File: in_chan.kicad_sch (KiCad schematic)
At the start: 7 parts, among them U7 MAX31910AUI+

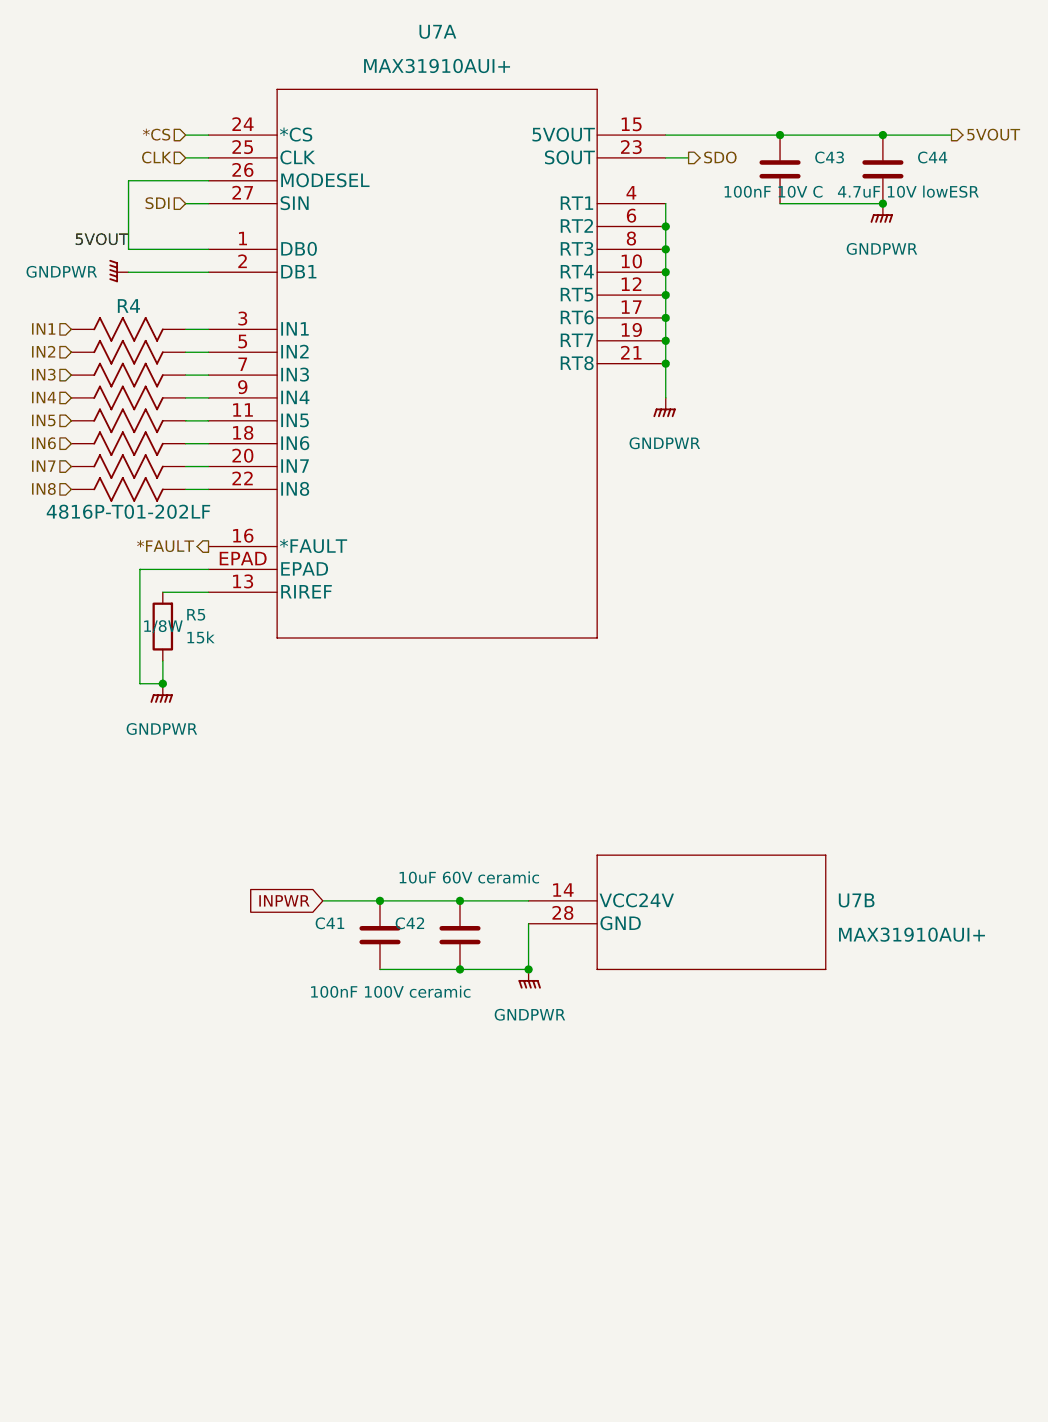
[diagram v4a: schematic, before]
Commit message: add zeners in the meantime, if the SPI isolator is delayed
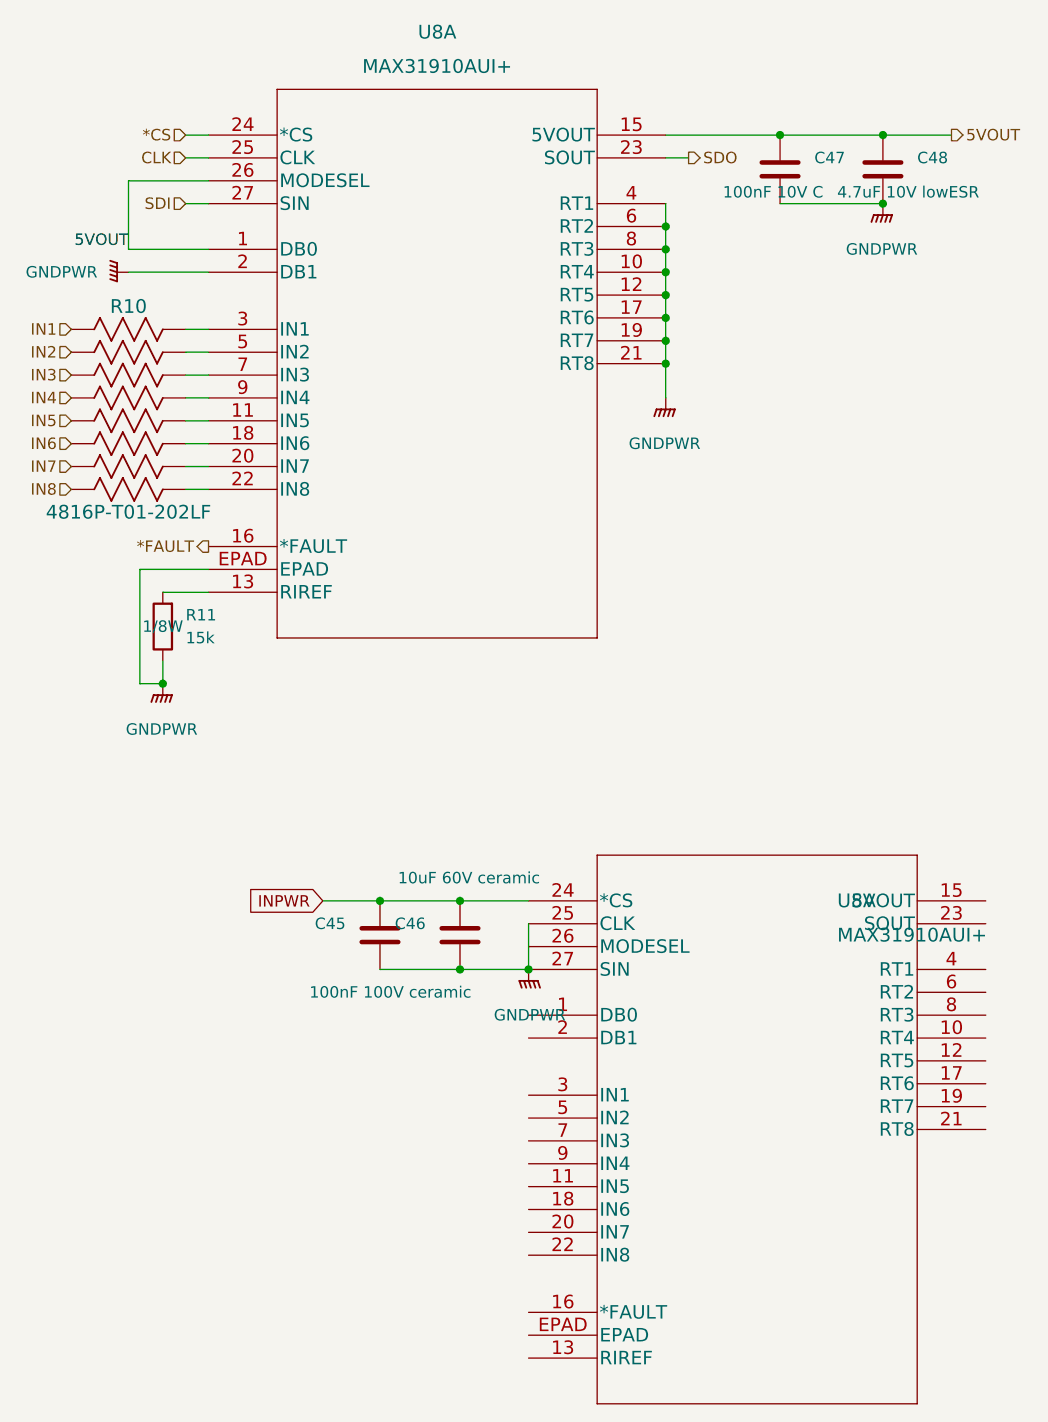
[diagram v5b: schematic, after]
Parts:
- renumbered C41 to C45, C42 to C46, C43 to C47, C44 to C48, R4 to R10, R5 to R11, U7 to U8
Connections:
- net GNDPWR: now also U8.25 (CLK), U8.27 (SIN); no longer U8.28 (GND)
- net INPWR: now also U8.24 (*CS); no longer U8.14 (VCC24V)

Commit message: fixes after V1
4 resistors for input power
disable CRCEN
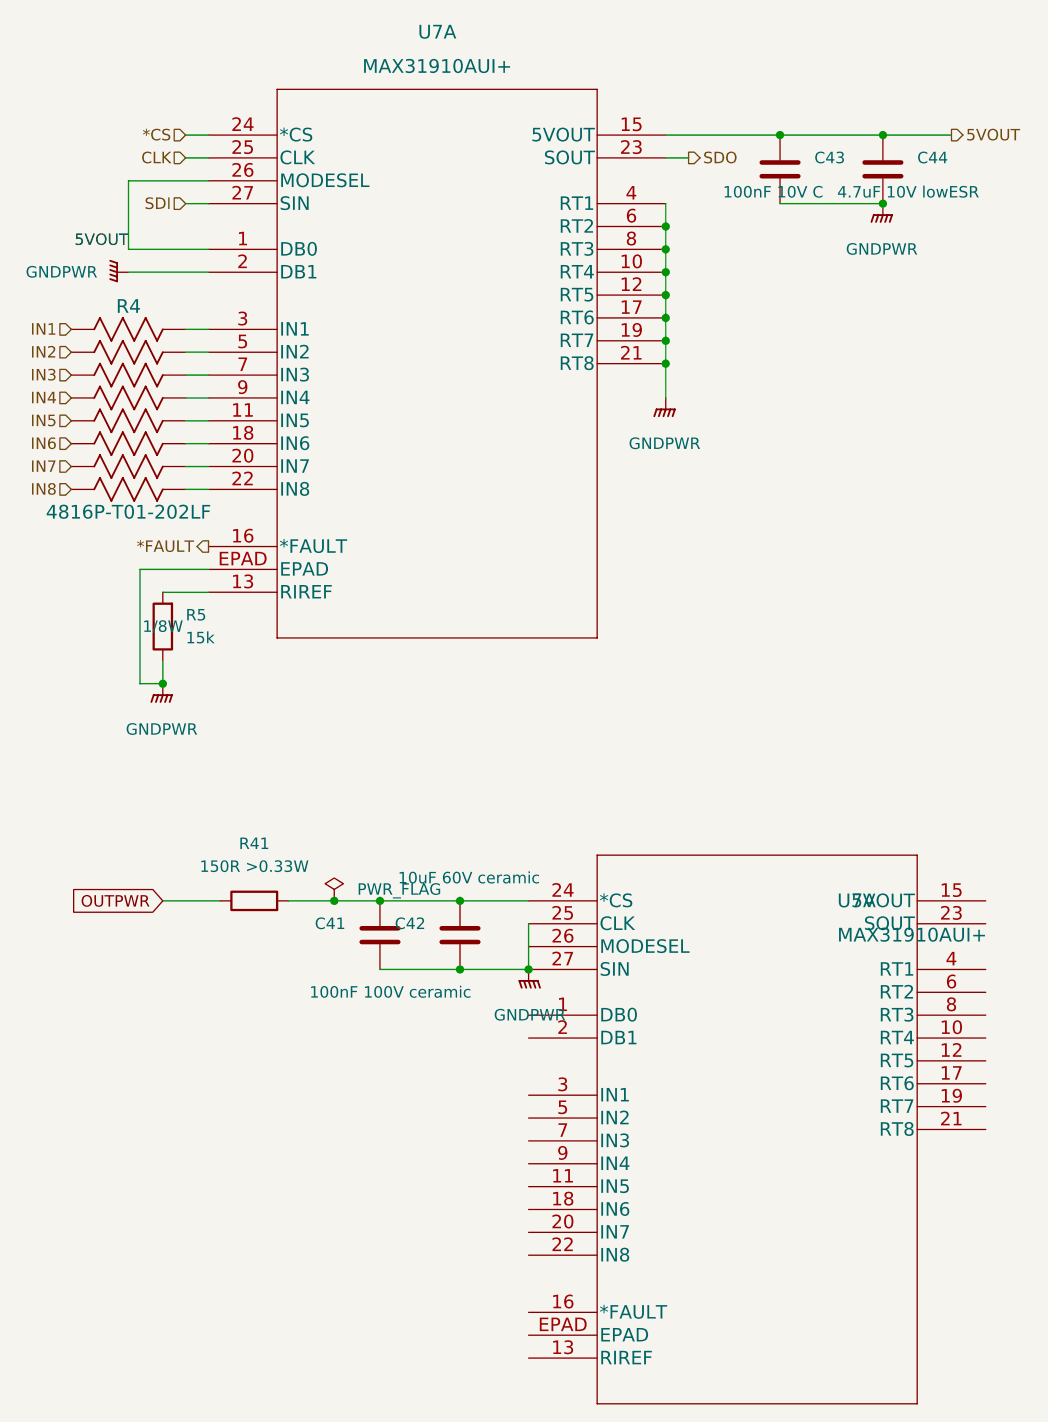
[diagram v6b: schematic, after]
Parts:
- added R41: 150R >0.33W, Resistor_SMD:R_1206_3216Metric, symbol Device:R
- renumbered C45 to C41, C46 to C42, C47 to C43, C48 to C44, R10 to R4, R11 to R5, U8 to U7
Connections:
- net INPWR: no longer names the net of C41.1, C42.1, U7.24 (*CS)
- net INPWR: now also R41.2
- new net OUTPWR: R41.1
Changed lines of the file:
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@@
   (junction (at 219.71 78.74) (diameter 0) (color 0 0 0 0)
   )
+  (junction (at 182.88 143.51) (diameter 0) (color 0 0 0 0)
+  )
   (junction (at 219.71 81.28) (diameter 0) (color 0 0 0 0)
   )
@@
     (stroke (width 0) (type default) (color 0 0 0 0))
   )
+  (wire (pts (xy 182.88 143.51) (xy 187.96 143.51))
+    (stroke (width 0) (type default) (color 0 0 0 0))
+  )
   (wire (pts (xy 166.37 80.01) (xy 168.91 80.01))
     (stroke (width 0) (type default) (color 0 0 0 0))
@@
     (stroke (width 0) (type default) (color 0 0 0 0))
   )
-  (wire (pts (xy 181.61 143.51) (xy 187.96 143.51))
+  (wire (pts (xy 163.83 143.51) (xy 170.18 143.51))
     (stroke (width 0) (type default) (color 0 0 0 0))
   )
@@
   )
   (wire (pts (xy 196.85 143.51) (xy 187.96 143.51))
+    (stroke (width 0) (type default) (color 0 0 0 0))
+  )
+  (wire (pts (xy 177.8 143.51) (xy 182.88 143.51))
     (stroke (width 0) (type default) (color 0 0 0 0))
   )
@@
     (effects (font (size 1.27 1.27)) (justify right bottom))
   )
-  (global_label "INPWR" (shape input) (at 181.61 143.51 180) (fields_autoplaced)
+  (global_label "OUTPWR" (shape input) (at 163.83 143.51 180) (fields_autoplaced)
     (effects (font (size 1.27 1.27)) (justify right))
-    (property "Intersheet References" "${INTERSHEET_REFS}" (id 0) (at 173.2702 143.4306 0)
+    (property "Intersheet References" "${INTERSHEET_REFS}" (id 0) (at 153.7969 143.4306 0)
       (effects (font (size 1.27 1.27)) (justify right) hide)
     )
@@
   (symbol (lib_id "power:GNDPWR") (at 163.83 119.38 0)
     (in_bom yes) (on_board yes) (fields_autoplaced)
-    (property "Reference" "#PWR051" (id 0) (at 163.83 124.46 0)
+    (property "Reference" "#PWR046" (id 0) (at 163.83 124.46 0)
       (effects (font (size 1.27 1.27)) hide)
     )
@@
   (symbol (lib_id "Device:R") (at 163.83 113.03 180)
     (in_bom yes) (on_board yes)
-    (property "Reference" "R11" (id 0) (at 166.37 111.76 0)
+    (property "Reference" "R5" (id 0) (at 166.37 111.76 0)
       (effects (font (size 1.27 1.27)) (justify right))
     )
@@
   (symbol (lib_id "power:GNDPWR") (at 204.47 151.13 0) (mirror y)
     (in_bom yes) (on_board yes) (fields_autoplaced)
-    (property "Reference" "#PWR052" (id 0) (at 204.47 156.21 0)
+    (property "Reference" "#PWR047" (id 0) (at 204.47 156.21 0)
       (effects (font (size 1.27 1.27)) hide)
     )
@@
     (pin "1")
   )
+  (symbol (lib_id "Device:R") (at 173.99 143.51 90)
+    (in_bom yes) (on_board yes) (fields_autoplaced)
+    (property "Reference" "R41" (id 0) (at 173.99 137.16 90))
+    (property "Value" "150R >0.33W" (id 1) (at 173.99 139.7 90))
+    (property "Footprint" "Resistor_SMD:R_1206_3216Metric" (id 2) (at 173.99 145.288 90)
+      (effects (font (size 1.27 1.27)) hide)
+    )
+    (property "Datasheet" "~" (id 3) (at 173.99 143.51 0)
+      (effects (font (size 1.27 1.27)) hide)
+    )
+    (pin "1")
+    (pin "2")
+  )
   (symbol (lib_id "power:GNDPWR") (at 243.84 66.04 0)
     (in_bom yes) (on_board yes) (fields_autoplaced)
-    (property "Reference" "#PWR054" (id 0) (at 243.84 71.12 0)
+    (property "Reference" "#PWR049" (id 0) (at 243.84 71.12 0)
       (effects (font (size 1.27 1.27)) hide)
     )
@@
   (symbol (lib_id "Device:C") (at 243.84 62.23 0)
     (in_bom yes) (on_board yes)
-    (property "Reference" "C48" (id 0) (at 247.65 60.9599 0)
+    (property "Reference" "C44" (id 0) (at 247.65 60.9599 0)
       (effects (font (size 1.27 1.27)) (justify left))
     )
@@
   (symbol (lib_id "Maxim industrial IO:MAX31910AUI+") (at 204.47 143.51 0)
     (in_bom yes) (on_board yes) (fields_autoplaced)
-    (property "Reference" "U8" (id 0) (at 238.76 143.51 0)
+    (property "Reference" "U7" (id 0) (at 238.76 143.51 0)
       (effects (font (size 1.524 1.524)) (justify left))
     )
@@
   (symbol (lib_id "Device:C") (at 187.96 147.32 0) (mirror y)
     (in_bom yes) (on_board yes)
-    (property "Reference" "C45" (id 0) (at 184.15 146.0499 0)
+    (property "Reference" "C41" (id 0) (at 184.15 146.0499 0)
       (effects (font (size 1.27 1.27)) (justify left))
     )
@@
   (symbol (lib_id "power:GNDPWR") (at 219.71 87.63 0)
     (in_bom yes) (on_board yes) (fields_autoplaced)
-    (property "Reference" "#PWR053" (id 0) (at 219.71 92.71 0)
+    (property "Reference" "#PWR048" (id 0) (at 219.71 92.71 0)
       (effects (font (size 1.27 1.27)) hide)
     )
@@
   (symbol (lib_id "Device:C") (at 232.41 62.23 0)
     (in_bom yes) (on_board yes)
-    (property "Reference" "C47" (id 0) (at 236.22 60.9599 0)
+    (property "Reference" "C43" (id 0) (at 236.22 60.9599 0)
       (effects (font (size 1.27 1.27)) (justify left))
     )
@@
   (symbol (lib_id "power:GNDPWR") (at 160.02 73.66 270)
     (in_bom yes) (on_board yes)
-    (property "Reference" "#PWR050" (id 0) (at 154.94 73.66 0)
+    (property "Reference" "#PWR045" (id 0) (at 154.94 73.66 0)
       (effects (font (size 1.27 1.27)) hide)
     )
@@
   (symbol (lib_id "Device:C") (at 196.85 147.32 0) (mirror y)
     (in_bom yes) (on_board yes)
-    (property "Reference" "C46" (id 0) (at 193.04 146.0499 0)
+    (property "Reference" "C42" (id 0) (at 193.04 146.0499 0)
       (effects (font (size 1.27 1.27)) (justify left))
     )
@@
   (symbol (lib_id "Num-IO:4816P-T01-103LF") (at 153.67 80.01 0)
     (in_bom yes) (on_board yes)
-    (property "Reference" "R10" (id 0) (at 160.02 77.47 0)
+    (property "Reference" "R4" (id 0) (at 160.02 77.47 0)
       (effects (font (size 1.524 1.524)))
     )
@@
   (symbol (lib_id "Maxim industrial IO:MAX31910AUI+") (at 168.91 58.42 0)
     (in_bom yes) (on_board yes) (fields_autoplaced)
-    (property "Reference" "U8" (id 0) (at 194.31 46.99 0)
+    (property "Reference" "U7" (id 0) (at 194.31 46.99 0)
       (effects (font (size 1.524 1.524)))
     )
@@
     (pin "EPAD")
   )
+  (symbol (lib_id "power:PWR_FLAG") (at 182.88 143.51 0)
+    (in_bom yes) (on_board yes) (fields_autoplaced)
+    (property "Reference" "#FLG0105" (id 0) (at 182.88 141.605 0)
+      (effects (font (size 1.27 1.27)) hide)
+    )
+    (property "Value" "PWR_FLAG" (id 1) (at 185.42 142.2399 0)
+      (effects (font (size 1.27 1.27)) (justify left))
+    )
+    (property "Footprint" "" (id 2) (at 182.88 143.51 0)
+      (effects (font (size 1.27 1.27)) hide)
+    )
+    (property "Datasheet" "~" (id 3) (at 182.88 143.51 0)
+      (effects (font (size 1.27 1.27)) hide)
+    )
+    (pin "1")
+  )
 )
